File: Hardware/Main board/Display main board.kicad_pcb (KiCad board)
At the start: 2 copper layers, 142.2 x 91.4 mm, 51 parts, among them J1 Board to Board, J3 Conn_01x03, P1 USB_C_Plug_USB2.0, U1 BQ25895RTW, U10 W25Q32JVSS, U4 RP2040, U5 AP7361C-33E, U6 AP7361C-33E, U7 AP7361C-33E, U8 AP7361C-33E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

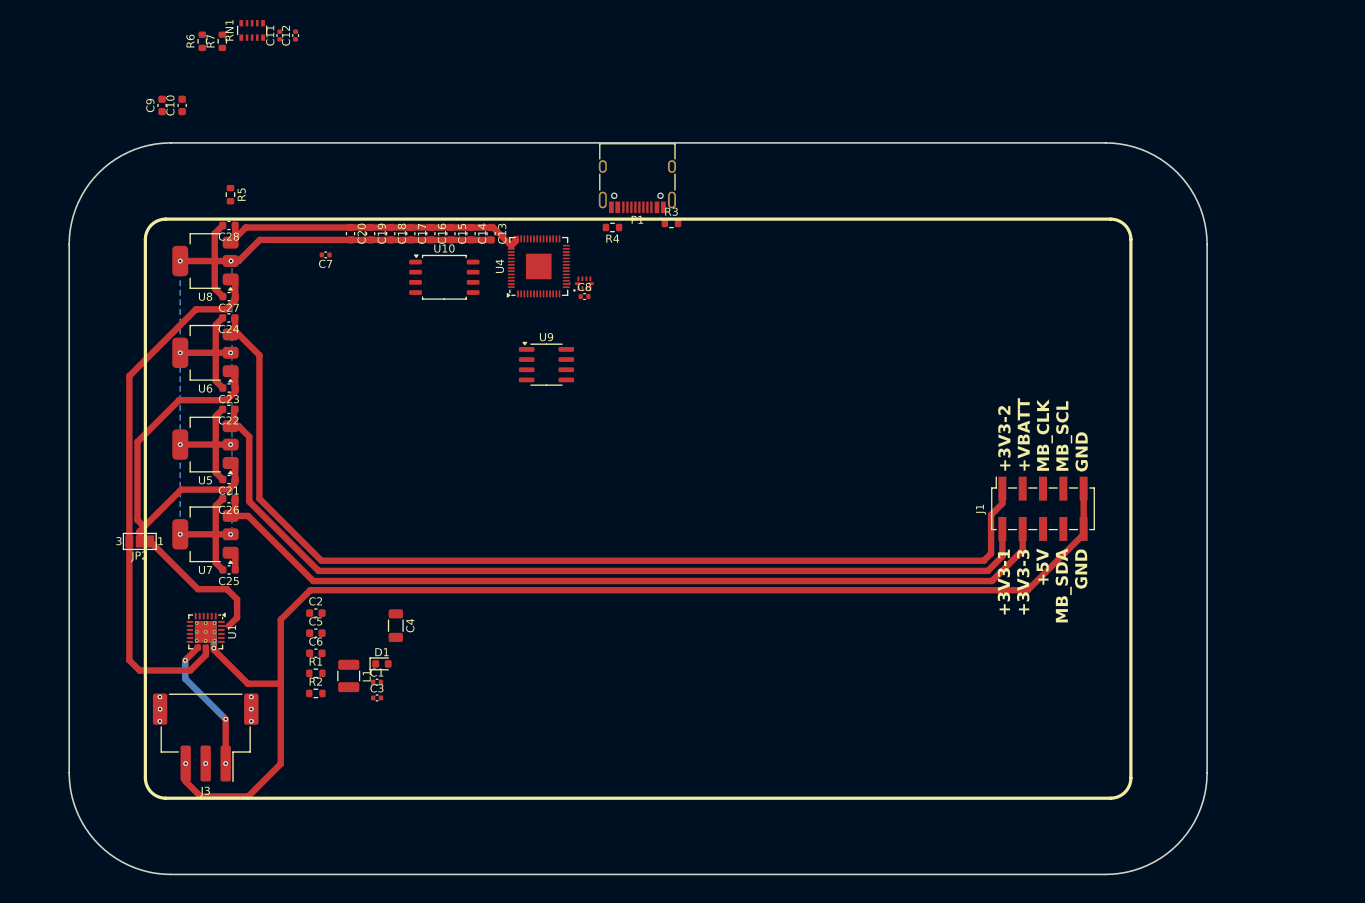
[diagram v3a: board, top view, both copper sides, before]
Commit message: 1st semi complete board layout
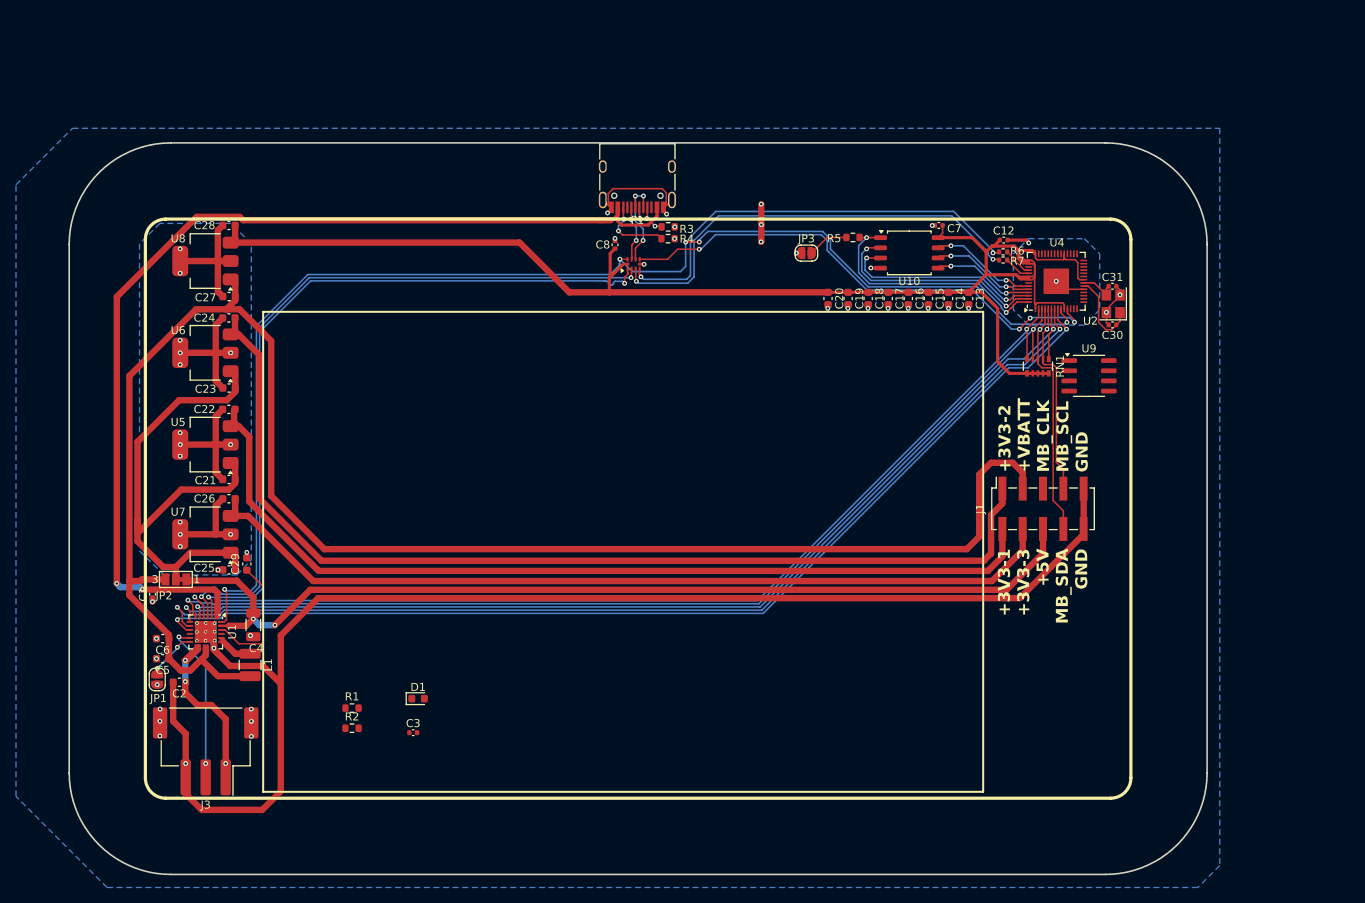
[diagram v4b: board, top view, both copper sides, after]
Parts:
- removed C10, C9: 10µF, Capacitor_SMD:C_0603_1608Metric
- removed C11: 1µF, Capacitor_SMD:C_0402_1005Metric
- added C29: 4.7μF, Capacitor_SMD:C_0603_1608Metric, F.Cu at (88.3, 103.5)
- added C30: 15pF, Capacitor_SMD:C_0402_1005Metric, F.Cu at (196.5, 73.6)
- added C31: 15pF, Capacitor_SMD:C_0402_1005Metric, F.Cu at (196.5, 68.8)
- added JP1: BMS_RESET, Jumper:SolderJumper-2_P1.3mm_Open_RoundedPad1.0x1.5mm, F.Cu at (77.1, 118.0)
- added JP3: USB_BOOT, Jumper:SolderJumper-2_P1.3mm_Open_RoundedPad1.0x1.5mm, F.Cu at (158.3, 64.7)
- added U2: ABM8-272-T3, Crystal:Crystal_SMD_Abracon_ABM8G-4Pin_3.2x2.5mm, F.Cu at (196.6, 71.0)
- R6, R7: footprint Resistor_SMD:R_0603_1608Metric -> Resistor_SMD:R_0402_1005Metric
- moved RN1 106.8 mm to (187.2, 78.8), turned to -90 degrees
- moved R6 103.8 mm to (182.9, 65.5), turned to 0 degrees
- moved R7 101.1 mm to (182.9, 64.5), turned to 180 degrees
- moved C12 92.1 mm to (183.0, 63.0), turned to 0 degrees
- moved R5 78.0 mm to (164.1, 62.7), turned to 0 degrees
- moved C7 76.7 mm to (174.8, 61.2)
- moved U9 67.8 mm to (193.6, 80.0)
- moved U4 64.7 mm to (189.5, 68.2)
- moved C13 60.2 mm to (178.6, 70.3)
- moved C16 60.2 mm to (171.0, 70.3)
- moved C19 60.2 mm to (163.5, 70.3)
- moved C14 60.2 mm to (176.1, 70.3)
- moved C15 60.2 mm to (173.5, 70.3)
- moved C17 60.2 mm to (168.5, 70.3)
- moved C18 60.2 mm to (166.0, 70.3)
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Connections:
- net Net-(U4-USB_DM) renamed /RP2040/D-
- net Net-(U4-USB_DP) renamed /RP2040/D+
- U4 pad 19: unconnected-(U4-TESTEN-Pad19) -> GND
- U4 pad 20: unconnected-(U4-XIN-Pad20) -> Net-(U4-XIN)
- U4 pad 21: unconnected-(U4-XOUT-Pad21) -> Net-(U4-XOUT)
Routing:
- net /USB_DSEL: track 0.00 -> 160.1 mm, vias 0 -> 5
- net +VBATT: track 67.4 -> 210.8 mm
- net +3.3V: track 40.2 -> 183.1 mm
- net /BMS_INT: track 0.00 -> 131.9 mm, vias 0 -> 2
- net /BMS_OTG: track 0.00 -> 131.6 mm, vias 0 -> 2
- net /BMS_CE: track 0.00 -> 131.4 mm, vias 0 -> 2
- net SYS_SDA: track 0.00 -> 128.8 mm, vias 0 -> 2
- net SYS_SCL: track 0.00 -> 127.0 mm, vias 0 -> 2
- net VBUS: track 0.00 -> 125.2 mm, vias 0 -> 2
- net +5V: track 18.5 -> 121.7 mm, vias 0 -> 2
- net /BMS_D-: track 0.00 -> 93.4 mm, vias 0 -> 2
- net /BMS_D+: track 0.00 -> 92.6 mm, vias 0 -> 2
- net /USB_DIS: track 0.00 -> 64.1 mm, vias 0 -> 4
- net /RP_D+: track 0.00 -> 55.7 mm, vias 0 -> 2
- net /RP_D-: track 0.00 -> 54.7 mm, vias 0 -> 2
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
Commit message: Forgot to route the TPM
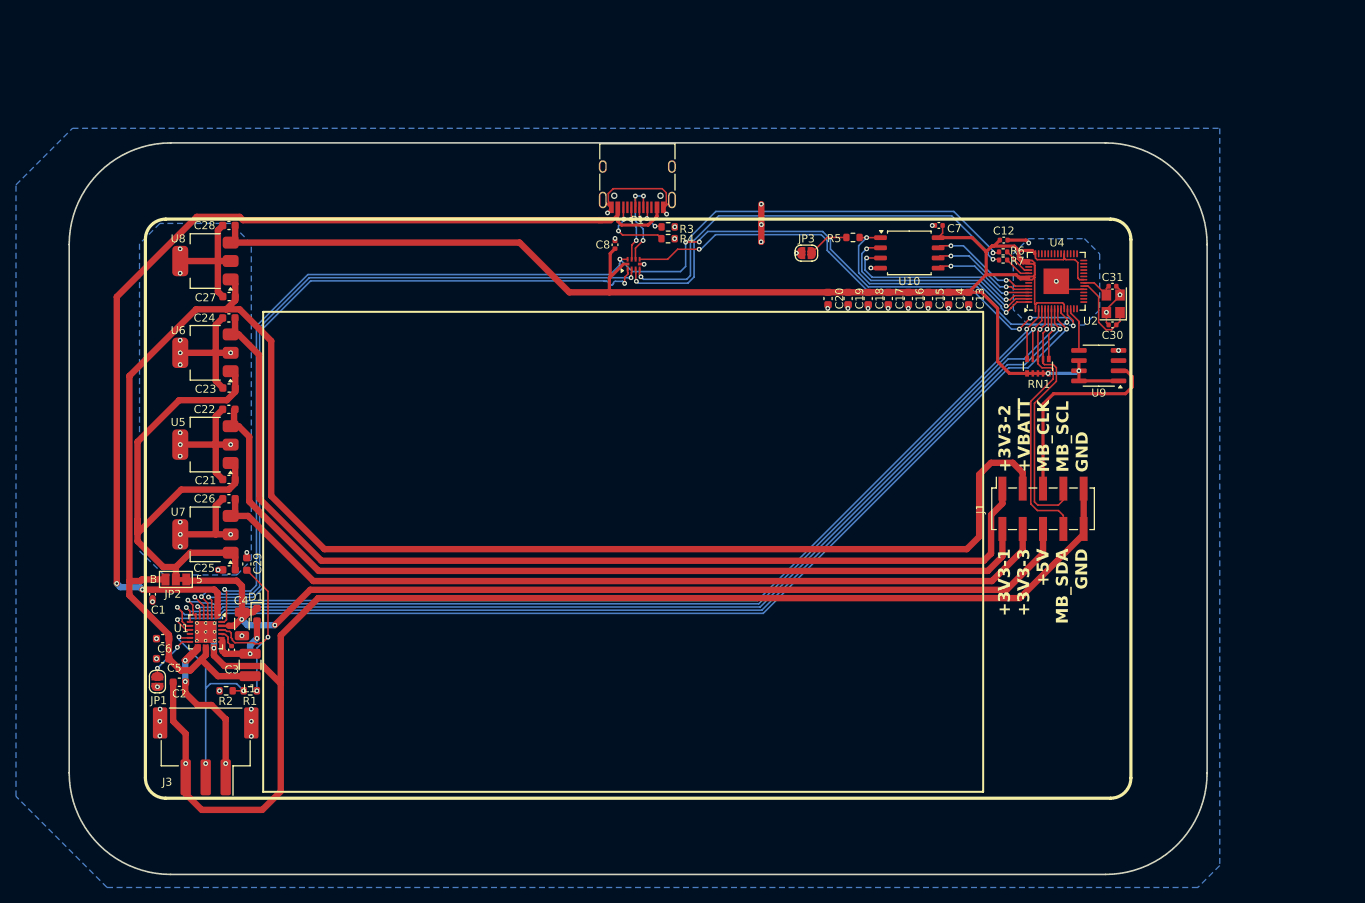
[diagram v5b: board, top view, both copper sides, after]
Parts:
- moved C3 25.0 mm to (86.4, 114.3), turned to -90 degrees
- moved D1 22.7 mm to (89.6, 109.9), turned to -90 degrees
- moved R2 16.4 mm to (85.8, 119.4), turned to 180 degrees
- moved R1 12.9 mm to (88.8, 119.4), turned to 180 degrees
- moved U9 1.76 mm to (194.8, 78.7), turned to 180 degrees
- moved C4 1.43 mm to (87.7, 111.0)
- moved JP1 0.27 mm to (77.2, 118.2)
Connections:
- U4 pad 12: /RP2040/IO9/MB_CLK -> MB_CLK_LOW
- U4 pad 23: +1V1 -> Net-(U4-DVDD-Pad23)
- U4 pad 45: +1V1 -> unconnected-(U4-VREG_VOUT-Pad45)
- U4 pad 50: +1V1 -> Net-(U4-DVDD-Pad23)
- U9 pad 1: unconnected-(U9-VM-Pad1) -> +3.3V
- U9 pad 2: unconnected-(U9-OUT1-Pad2) -> MB_CLK
- U9 pad 4: Net-(U9-GND-Pad4) -> GND
- U9 pad 5: unconnected-(U9-IN2-Pad5) -> MB_CLK_LOW
- U9 pad 6: unconnected-(U9-IN1-Pad6) -> +3.3V
- U9 pad 7: unconnected-(U9-~{SLEEP}-Pad7) -> +3.3V
- U9 pad 8: unconnected-(U9-VCC-Pad8) -> +3.3V
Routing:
- net MB_CLK: track 0.00 -> 25.9 mm
- net +3.3V: track 183.1 -> 194.6 mm, vias 0 -> 2
- net Net-(U1-REGN): track 15.8 -> 24.1 mm, vias 0 -> 2
- net MB_SCL: track 24.4 -> 32.3 mm
- net /BMS/NTC: track 18.6 -> 25.4 mm, vias 2 -> 3
- net MB_CLK_LOW: track 0.00 -> 5.64 mm
- net Net-(D1-A): track 4.13 -> 9.30 mm, vias 0 -> 2
- net MB_SDA: track 29.9 -> 33.8 mm
- net +5V: track 121.7 -> 124.4 mm
- net Net-(U1-BTST): track 0.00 -> 2.30 mm
- net /USB_DIS: track 64.1 -> 64.8 mm
- net GND: track 267.9 -> 268.3 mm, vias 47 -> 49

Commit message: Add resistor for ILIM pin
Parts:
- added R8: 260, Resistor_SMD:R_0402_1005Metric, F.Cu at (78.2, 109.6)
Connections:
- U1 pad 10: unconnected-(U1-ILIM-Pad10) -> Net-(U1-ILIM)
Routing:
- net Net-(U1-ILIM): track 0.00 -> 3.90 mm
- net GND: track 268.3 -> 268.8 mm, vias 49 -> 50

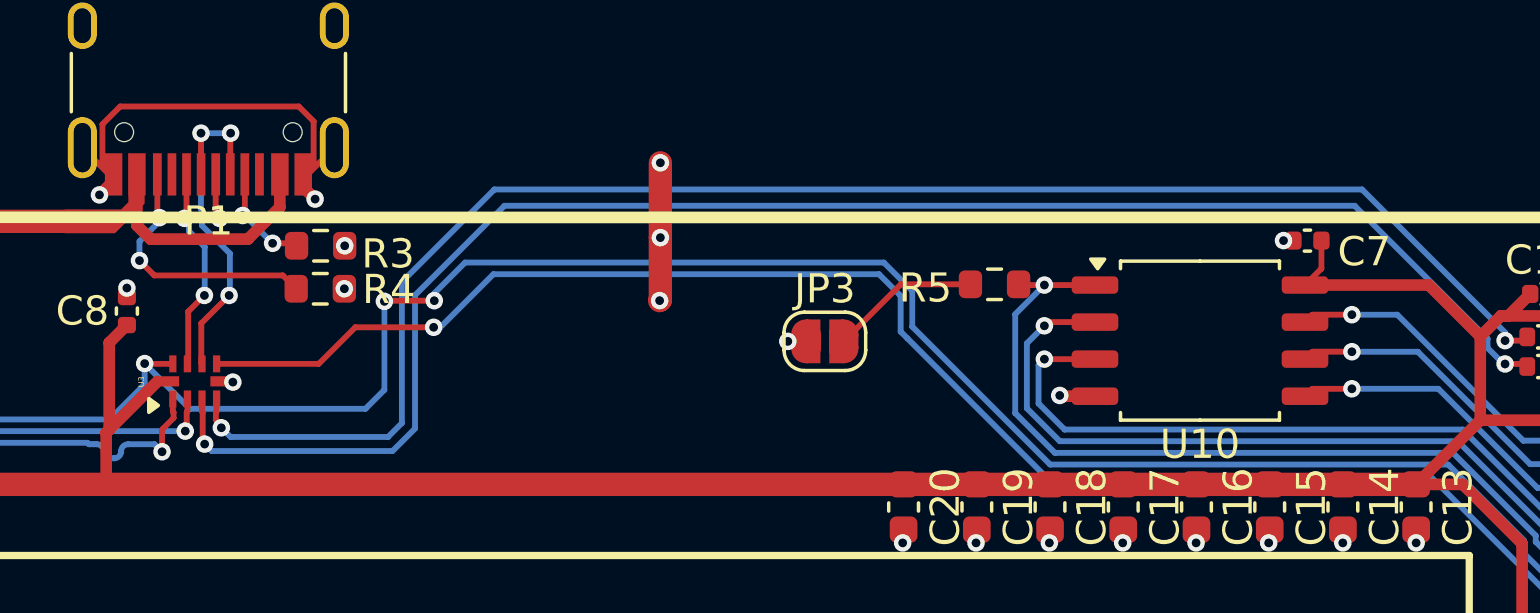
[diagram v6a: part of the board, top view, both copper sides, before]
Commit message: Diff Pair matching
matched all USB lines to be within 1mm of length to each other
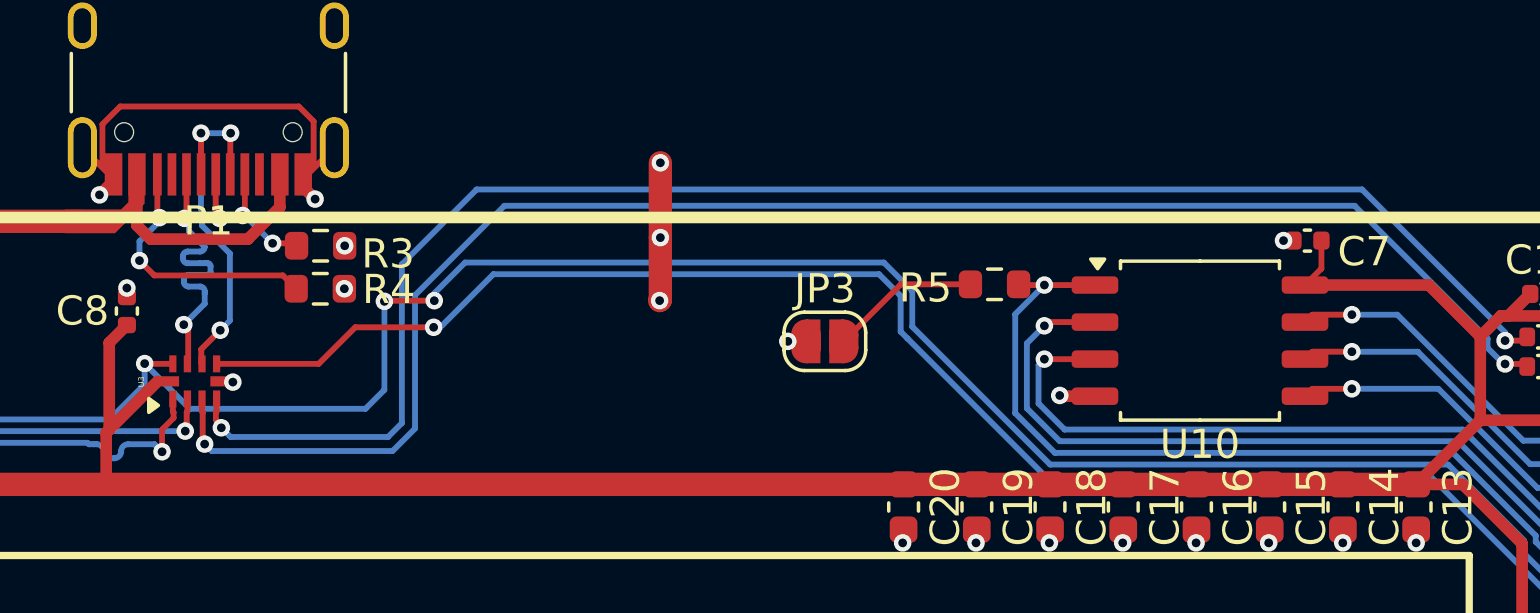
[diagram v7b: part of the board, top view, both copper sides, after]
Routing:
- net /USB_D+: track 9.82 -> 12.7 mm

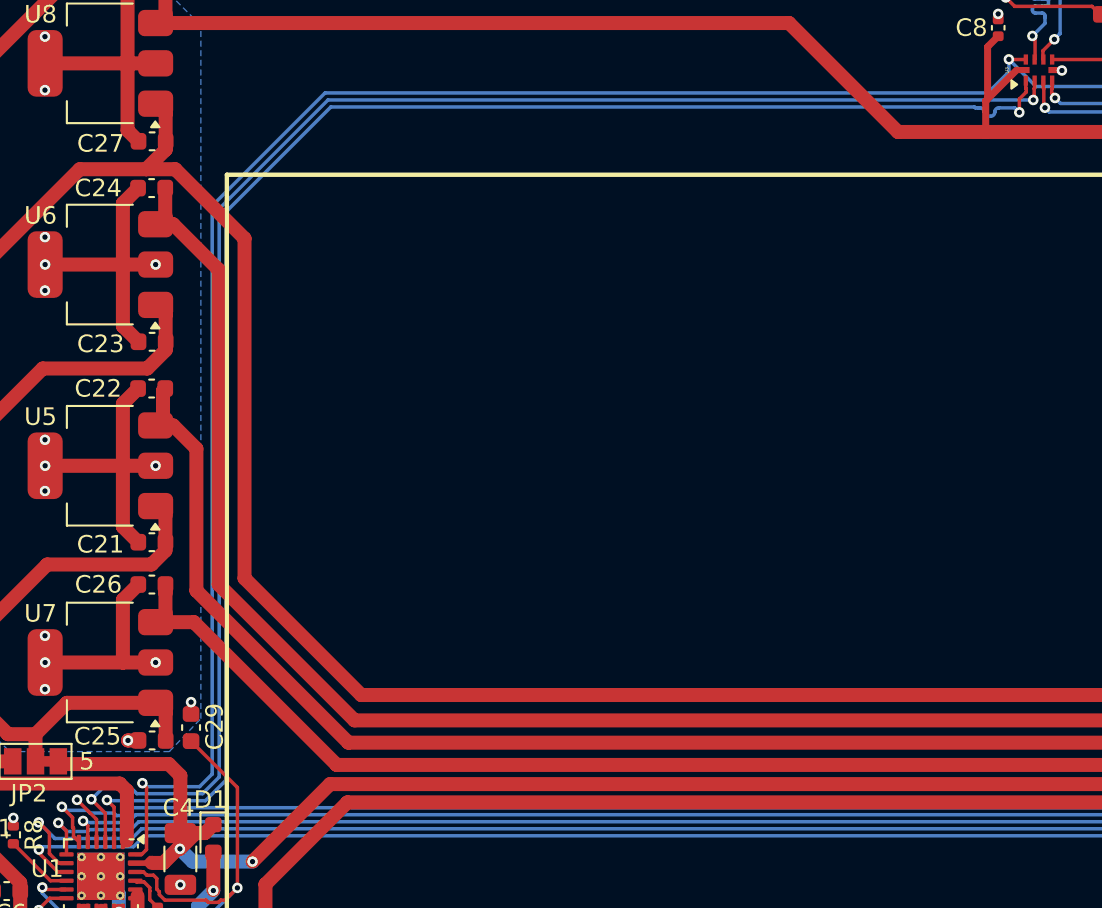
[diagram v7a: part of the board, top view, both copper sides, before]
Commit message: more diff pair matching, fixed BMD Data lines
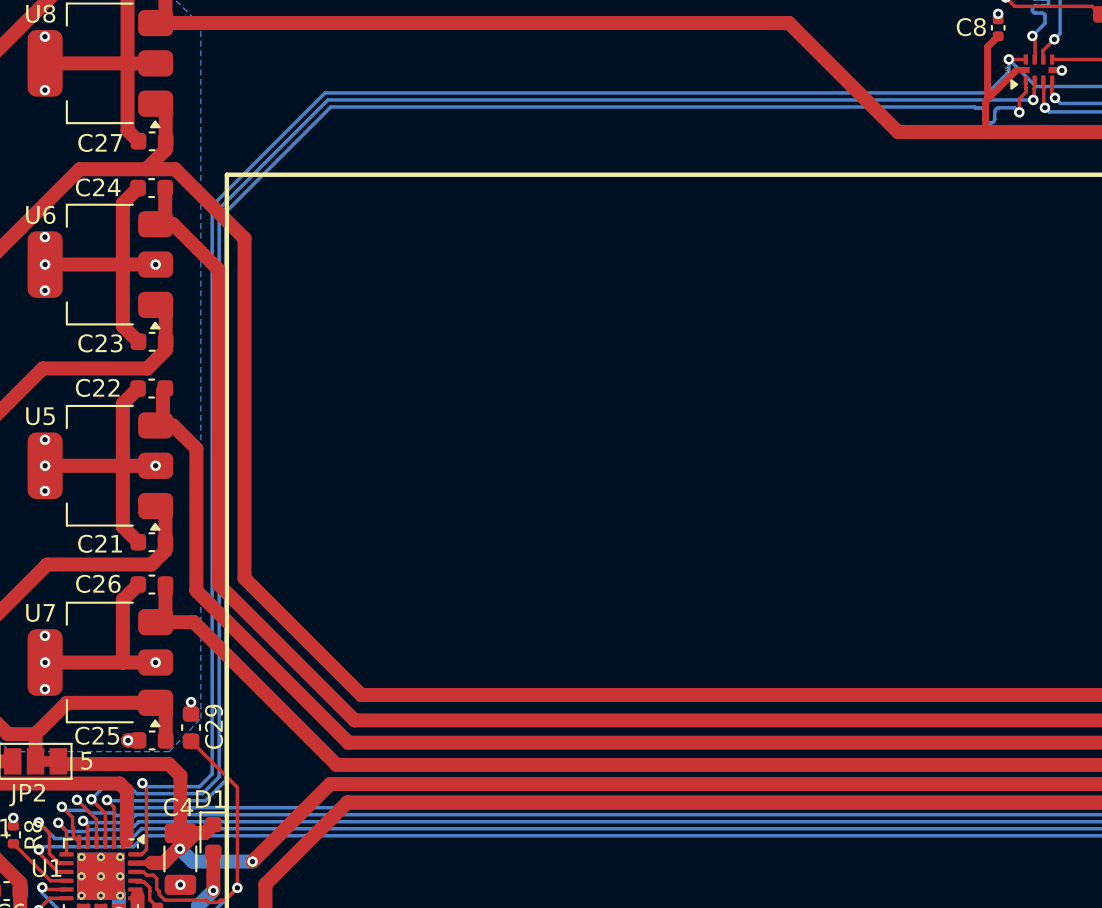
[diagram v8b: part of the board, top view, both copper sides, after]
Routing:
- net /BMS_D+: track 92.6 -> 93.4 mm
